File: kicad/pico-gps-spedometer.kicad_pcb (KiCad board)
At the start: 2 copper layers, 88.1 x 75.5 mm, 25 parts, among them J1 Akkumulátor be, J2 TP4056-18650-Charger, J3 uBlox NEO GPS (6M/8M), Q1 PN2222A, U1 RP2040-ZERO, U2 DS18B20, U3 LM7805_TO220, U4 TFT_320x240

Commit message: Refactor code structure for improved readability and maintainability
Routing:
- net +5VBATT: track 152.5 -> 153.6 mm
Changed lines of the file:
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@@
 		(tags "C Disc series Radial pin pitch 2.50mm diameter 5mm width 2.5mm Capacitor")
 		(property "Reference" "C1"
-			(at 1 2.25 90)
+			(at 1.4025 -2.68 90)
 			(layer "F.SilkS")
 			(effects
@@
 	)
 	(segment
+		(start 113.9175 48.89)
+		(end 113.9175 71.165)
+		(width 1)
+		(layer "F.Cu")
+		(net 3)
+	)
+	(segment
+		(start 75.43 74.4025)
+		(end 72.68 71.6525)
+		(width 1)
+		(layer "F.Cu")
+		(net 3)
+	)
+	(segment
 		(start 67.68 24.9025)
 		(end 66.805 25.7775)
@@
 	)
 	(segment
-		(start 72.68 63.0275)
-		(end 75.305 60.4025)
+		(start 113.9175 71.165)
+		(end 110.68 74.4025)
 		(width 1)
 		(layer "F.Cu")
@@
 	)
 	(segment
-		(start 75.43 74.4025)
-		(end 72.68 71.6525)
-		(width 1)
-		(layer "F.Cu")
-		(net 3)
-	)
-	(segment
 		(start 87.43 39.9025)
 		(end 86.305 38.7775)
@@
 	)
 	(segment
+		(start 72.68 71.6525)
+		(end 72.68 57.82)
+		(width 1)
+		(layer "F.Cu")
+		(net 3)
+	)
+	(segment
 		(start 66.805 27.6525)
 		(end 66.805 27.9025)
@@
 	)
 	(segment
-		(start 113.9175 48.89)
-		(end 113.9175 71.165)
+		(start 72.68 57.82)
+		(end 73.3975 57.1025)
 		(width 1)
 		(layer "F.Cu")
@@
 	)
 	(segment
-		(start 113.9175 71.165)
-		(end 110.68 74.4025)
-		(width 1)
-		(layer "F.Cu")
-		(net 3)
-	)
-	(segment
-		(start 75.305 60.4025)
+		(start 73.3975 57.1025)
 		(end 75.305 57.1025)
-		(width 1)
-		(layer "F.Cu")
-		(net 3)
-	)
-	(segment
-		(start 72.68 71.6525)
-		(end 72.68 63.0275)
 		(width 1)
 		(layer "F.Cu")
@@
 	)
 	(segment
-		(start 125.885 27.6075)
-		(end 131.555 33.2775)
+		(start 125.885 30.635)
+		(end 131.555 36.305)
 		(width 1)
 		(layer "B.Cu")
@@
 	)
 	(segment
-		(start 131.555 33.2775)
-		(end 131.555 41.4025)
-		(width 1)
-		(layer "B.Cu")
-		(net 7)
-	)
-	(segment
 		(start 129.18 67.6525)
 		(end 130.68 67.6525)
@@
 	)
 	(segment
-		(start 125.885 27.6075)
-		(end 125.885 25.9025)
+		(start 125.885 25.9025)
+		(end 125.885 30.635)
 		(width 1)
 		(layer "B.Cu")
@@
 	)
 	(segment
+		(start 131.555 36.305)
+		(end 131.555 41.4025)
+		(width 1)
+		(layer "B.Cu")
+		(net 7)
+	)
+	(segment
 		(start 137.055 26.1525)
 		(end 131.685 26.1525)
@@
 	)
 	(segment
-		(start 84.43 62.6525)
+		(start 84.43 62.18)
 		(end 84.43 60.7125)
-		(width 0.2)
-		(layer "B.Cu")
-		(net 16)
-	)
-	(segment
-		(start 85.285 64.6525)
-		(end 85.285 63.5075)
 		(width 0.2)
 		(layer "B.Cu")
@@
 	)
 	(segment
-		(start 85.285 63.5075)
-		(end 84.43 62.6525)
+		(start 85.285 64.6525)
+		(end 85.285 63.035)
+		(width 0.2)
+		(layer "B.Cu")
+		(net 16)
+	)
+	(segment
+		(start 85.285 63.035)
+		(end 84.43 62.18)
 		(width 0.2)
 		(layer "B.Cu")
@@
 	)
 	(segment
-		(start 79.505 50.4825)
-		(end 82.115 53.0925)
+		(start 79.505 51.255)
+		(end 81.3425 53.0925)
 		(width 0.2)
 		(layer "B.Cu")
@@
 	)
 	(segment
-		(start 82.115 53.0925)
+		(start 81.3425 53.0925)
 		(end 84.43 53.0925)
 		(width 0.2)
@@
 	(segment
 		(start 79.505 47.9725)
-		(end 79.505 50.4825)
-		(width 0.2)
-		(layer "B.Cu")
+		(end 79.505 51.255)
+		(width 0.2)
+		(layer "B.Cu")

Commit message: Refactor code structure for improved readability and maintainability
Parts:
- added Q2: BC212, Package_TO_SOT_THT:TO-92_Inline, F.Cu at (70.2, 58.5)
- added R7: 390, Resistor_THT:R_Axial_DIN0204_L3.6mm_D1.6mm_P7.62mm_Horizontal, F.Cu at (66.2, 72.2)
- added R8: 4k7, Resistor_THT:R_Axial_DIN0204_L3.6mm_D1.6mm_P7.62mm_Horizontal, F.Cu at (75.8, 60.9)
- moved BZ1 15.1 mm to (75.2, 72.2), turned to 90 degrees
- moved J3 3.19 mm to (57.0, 78.3)
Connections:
- U1 pad 2: /LED -> Net-(U1-GP1)
- U4 pad 8: /LED -> Net-(Q2-C)
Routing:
- net Net-(Q2-C): track 0.00 -> 40.4 mm
- net /LED: track 37.0 -> 0.00 mm
- net Net-(U1-GP1): track 0.00 -> 31.8 mm
- net GND: track 303.7 -> 332.4 mm
- net +5VBATT: track 153.6 -> 142.8 mm
- net /SCK: track 51.6 -> 42.6 mm
- net Net-(Q2-E): track 0.00 -> 6.78 mm
- net Net-(Q2-B): track 0.00 -> 5.85 mm
- net GPS_TXD: track 39.0 -> 41.5 mm
- net GPS_RXD: track 42.3 -> 44.9 mm
- net /MISO: track 67.7 -> 65.3 mm
- net +3V3: track 113.7 -> 115.9 mm
- net Net-(U1-GP8): track 37.1 -> 35.3 mm
- net Net-(BT1-2): track 81.7 -> 80.7 mm
- net Net-(U1-GP27): track 63.1 -> 63.9 mm

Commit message: Refactor code structure for improved readability and maintainability
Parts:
- added ?: , , F.Cu at (99.5, 86.4)
- added REF**: MountingHole_2.2mm_M2, MountingHole:MountingHole_2.2mm_M2, F.Cu at (57.0, 96.0)
- added REF**: MountingHole_2.2mm_M2, MountingHole:MountingHole_2.2mm_M2, F.Cu at (130.5, 72.2)
- D1: footprint Diode_THT:D_DO-15_P15.24mm_Horizontal -> Diode_THT:D_DO-41_SOD81_P10.16mm_Horizontal
- moved REF** 25.0 mm to (62.0, 70.5)
- moved REF** 19.9 mm to (138.0, 26.5)
- moved J1 11.4 mm to (138.2, 37.5), turned to 180 degrees
- moved REF** 6.32 mm to (62.0, 26.5)
- moved D1 6.23 mm to (131.5, 47.8)
- moved J3 3.08 mm to (57.0, 81.4)
- moved REF** 2.88 mm to (138.0, 70.5)
- moved R7 1.50 mm to (67.8, 72.3)
- moved BZ1 0.76 mm to (76.0, 72.1)
- moved R8 0.50 mm to (76.2, 60.9)
- moved U1 0.45 mm to (74.9, 37.8)
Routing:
- net GND: track 332.4 -> 343.4 mm
- net GPS_TXD: track 41.5 -> 44.8 mm
- net GPS_RXD: track 44.9 -> 48.1 mm
- net +3V3: track 115.9 -> 118.9 mm
- net /MISO: track 65.3 -> 63.2 mm
- net +5VBATT: track 142.8 -> 141.5 mm
- net Net-(D1-A): track 5.55 -> 6.78 mm
- net Net-(Q2-E): track 6.78 -> 5.75 mm
- net Net-(U1-GP1): track 31.8 -> 31.1 mm
- net /T_CS: track 53.1 -> 52.5 mm
- net Net-(Q2-B): track 5.85 -> 6.46 mm
- net Net-(BZ1--): track 8.73 -> 8.15 mm
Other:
- board size 88.1 x 75.5 mm -> 89 x 76 mm

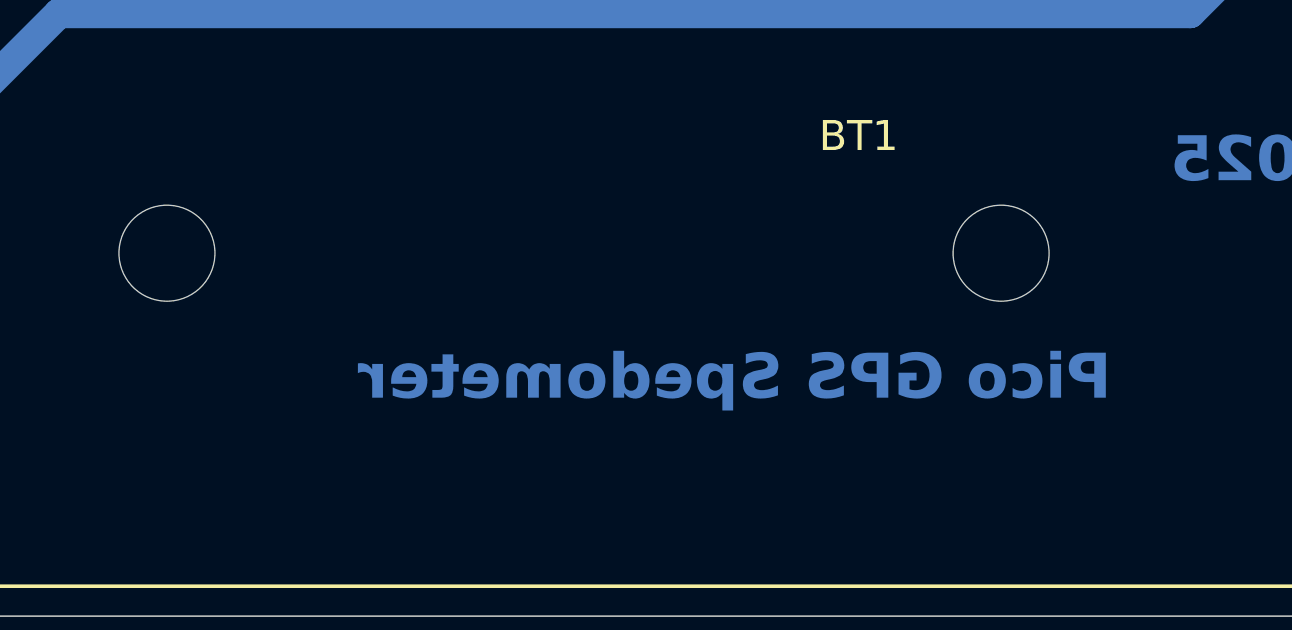
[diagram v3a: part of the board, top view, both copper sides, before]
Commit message: Refactor power net naming and update schematic properties
- Changed net name from "+5VBATT" to "+BATT" in PCB and schematic files for consistency.
- Updated various properties in the schematic to reflect the new net name.
- Adjusted positions of certain properties for better alignment and readability.
- Corrected the spelling of "Speedometer" in the PCB file.
- Modified resistor value from "22k" to "15k" in the PCB file.
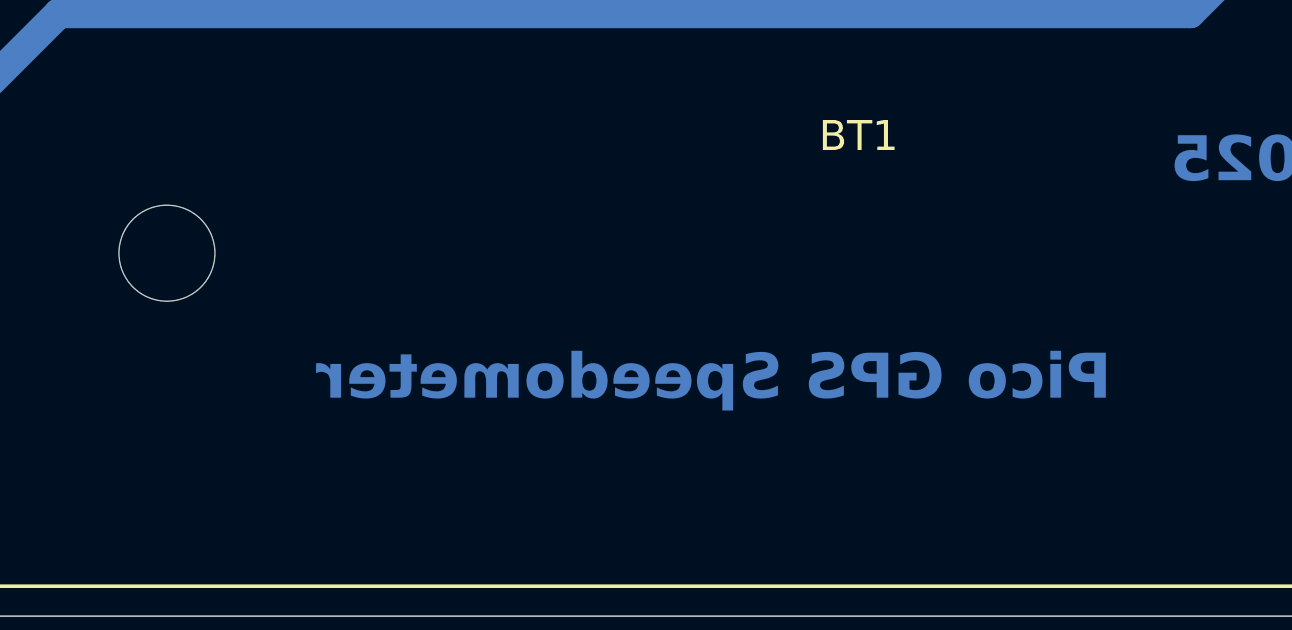
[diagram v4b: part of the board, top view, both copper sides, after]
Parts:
- removed ?: , 
- R2: value 22k -> 15k
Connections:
- net +5VBATT renamed +BATT
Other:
- board text added: "Pico GPS Speedometer"
- board text removed: "Pico GPS Spedometer"
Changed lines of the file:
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@@
 	(net 1 "Net-(BT1-1)")
 	(net 2 "Net-(BT1-2)")
-	(net 3 "+5VBATT")
+	(net 3 "+BATT")
 	(net 4 "Net-(BZ1--)")
 	(net 5 "+5V")
@@
 		(embedded_fonts no)
 	)
-	(footprint ""
-		(layer "F.Cu")
-		(at 99.5 86.4025)
-		(property "Reference" ""
-			(at 0 0 0)
-			(layer "F.SilkS")
-			(effects
-				(font
-					(size 1.27 1.27)
-					(thickness 0.15)
-				)
-			)
-		)
-		(property "Value" ""
-			(at 0 0 0)
-			(layer "F.Fab")
-			(effects
-				(font
-					(size 1.27 1.27)
-					(thickness 0.15)
-				)
-			)
-		)
-		(property "Datasheet" ""
-			(at 0 0 0)
-			(layer "F.Fab")
-			(hide yes)
-			(effects
-				(font
-					(size 1.27 1.27)
-					(thickness 0.15)
-				)
-			)
-		)
-		(property "Description" ""
-			(at 0 0 0)
-			(layer "F.Fab")
-			(hide yes)
-			(effects
-				(font
-					(size 1.27 1.27)
-					(thickness 0.15)
-				)
-			)
-		)
-		(pad "" np_thru_hole circle
-			(at 0 0 180)
-			(size 3.2 3.2)
-			(drill 3.2)
-			(layers "*.Cu" "*.Mask")
-		)
-		(embedded_fonts no)
-	)
 	(footprint "Diode_THT:D_DO-41_SOD81_P10.16mm_Horizontal"
 		(layer "F.Cu")
@@
 			(layers "*.Cu" "*.Mask")
 			(remove_unused_layers no)
-			(net 3 "+5VBATT")
+			(net 3 "+BATT")
 			(pintype "passive")
 		)
@@
 			(layers "*.Cu" "*.Mask")
 			(remove_unused_layers no)
-			(net 3 "+5VBATT")
+			(net 3 "+BATT")
 			(pinfunction "+")
 			(pintype "passive")
@@
 			(layers "*.Cu" "*.Mask")
 			(remove_unused_layers no)
-			(net 3 "+5VBATT")
+			(net 3 "+BATT")
 			(pinfunction "5V")
 			(pintype "power_in")
@@
 			(layers "*.Cu" "*.Mask")
 			(remove_unused_layers no)
-			(net 3 "+5VBATT")
+			(net 3 "+BATT")
 			(pinfunction "Pin_3")
 			(pintype "passive")
@@
 			)
 		)
-		(property "Value" "22k"
+		(property "Value" "15k"
 			(at 3.81 1.92 90)
 			(layer "F.Fab")
@@
 		(layer "Edge.Cuts")
 	)
-	(gr_text "Pico GPS Spedometer"
+	(gr_text "Pico GPS Speedometer"
 		(at 103.18 91.4025 0)
 		(layer "B.Cu")
